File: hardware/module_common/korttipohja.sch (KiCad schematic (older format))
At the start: 6 parts

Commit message: Add root PCB for module design.
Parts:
- removed J?: Conn_01x07_Female, symbol Connector:Conn_01x07_Female
- removed J?: Conn_01x02_Female, symbol Connector:Conn_01x02_Female
- added U1: WAVGAT_CAN, WAVGAT_CAN:WAVGAT_CAN, symbol WAVGAT_CAN:WAVGAT_CAN
- J1: renamed from J?; footprint (none) -> Connector_RJ:RJ45_BEL_SS74301-00x_Vertical
- R1, R2: renamed from R?; footprint (none) -> Resistor_SMD:R_0603_1608Metric_Pad1.05x0.95mm_HandSolder
- gave numbers to parts that had none: 1
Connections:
- wire segments 51 -> 57
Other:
- moved on the sheet: A1, J1, R1, R2

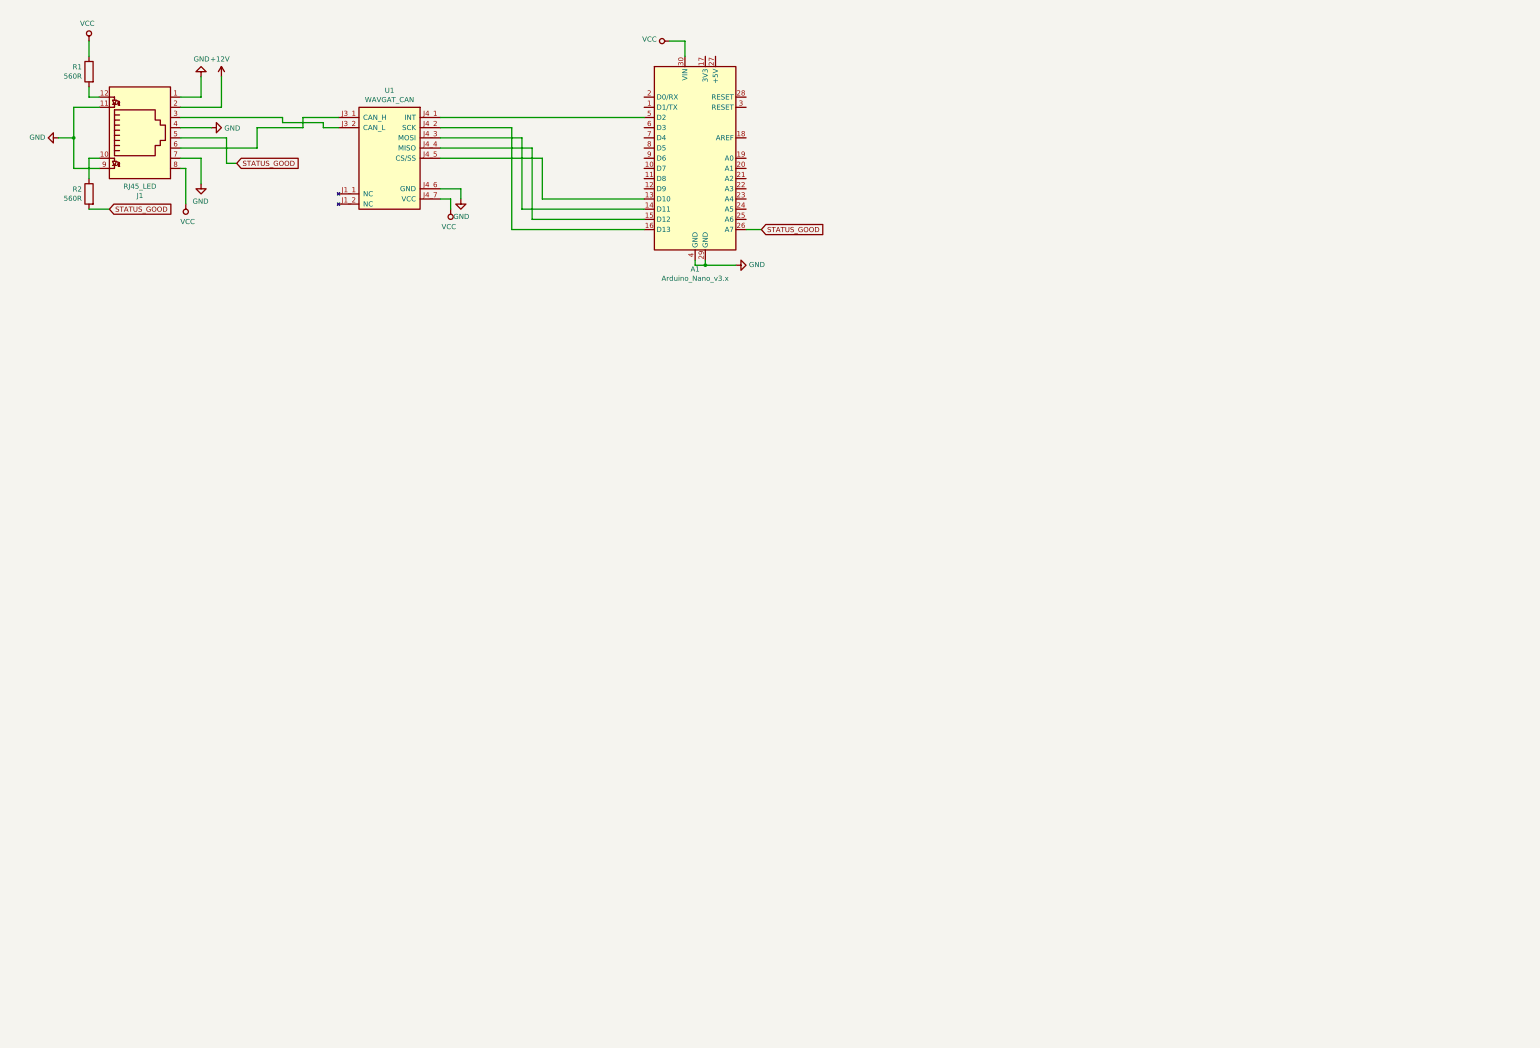
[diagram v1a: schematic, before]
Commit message: Finish first iteration of module common backplane
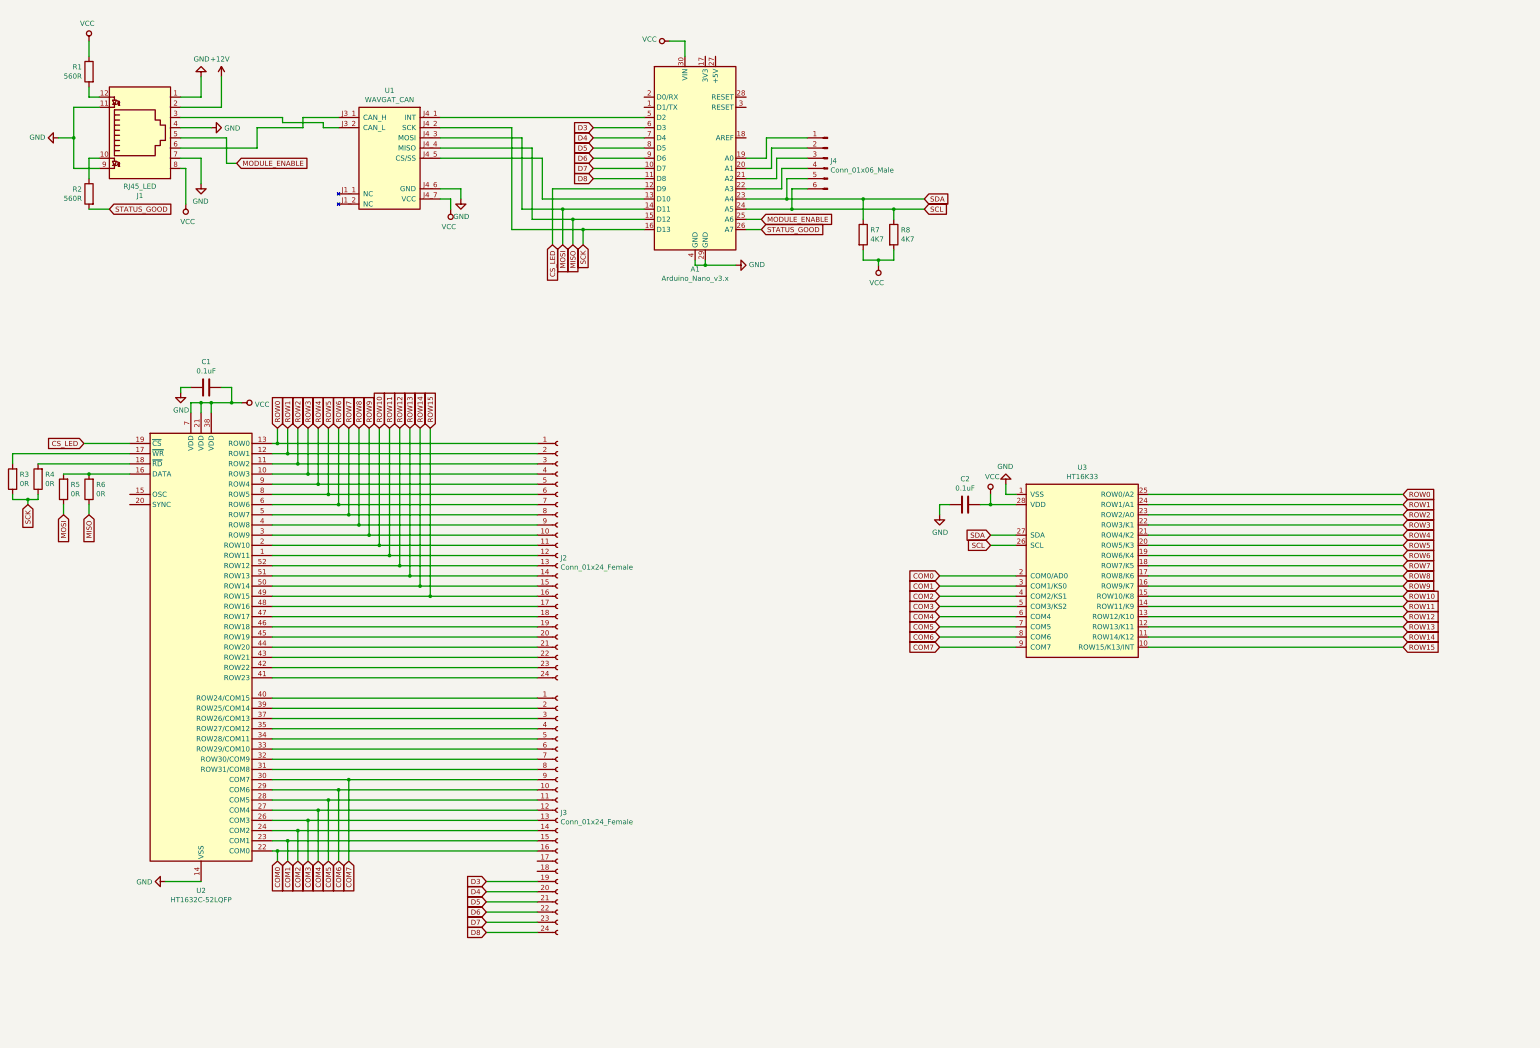
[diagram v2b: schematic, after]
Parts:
- added C1, C2: 0.1uF, Capacitor_SMD:C_0603_1608Metric_Pad1.05x0.95mm_HandSolder, symbol Device:C
- added J2, J3: Conn_01x24_Female, Connector_PinHeader_2.54mm:PinHeader_1x24_P2.54mm_Vertical, symbol Connector:Conn_01x24_Female
- added J4: Conn_01x06_Male, Connector_PinHeader_2.54mm:PinHeader_1x06_P2.54mm_Vertical, symbol Connector:Conn_01x06_Male
- added R3, R4, R5, R6: 0R, Resistor_SMD:R_0603_1608Metric_Pad1.05x0.95mm_HandSolder, symbol Device:R
- added R7, R8: 4K7, Resistor_SMD:R_0603_1608Metric_Pad1.05x0.95mm_HandSolder, symbol Device:R
- added U2: HT1632C-52LQFP, Package_QFP:LQFP-52_14x14mm_P1mm, symbol Driver_LED:HT1632C-52LQFP
- added U3: HT16K33, Package_SO:SOIC-28W_7.5x17.9mm_P1.27mm, symbol ProjectChips:HT16K33
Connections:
- net GND: now also C1.2, C2.2, U2.14 (VSS), U2.25 (VSS), U2.36 (VSS), U3.1 (VSS)
- net STATUS_GOOD: no longer J1.5
- net VCC: now also C1.1, C2.1, R7.2, R8.2, U2.21 (VDD), U2.38 (VDD), U2.7 (VDD), U3.28 (VDD)
- net D7: now reaches A1.10 (D7)
- net D7: now also J3.23 (Pin_23)
- net D8: now reaches A1.11 (D8)
- net D8: now also J3.24 (Pin_24)
- net CS_LED: now reaches A1.12 (D9)
- net CS_LED: now also U2.19 (~CS)
- net MOSI: now reaches A1.14 (D11), U1.J4_3 (MOSI)
- net MOSI: now also R5.1
- net MISO: now reaches A1.15 (D12), U1.J4_4 (MISO)
- net MISO: now also R6.1
- net SCK: now reaches A1.16 (D13), U1.J4_2 (SCK)
- net SCK: now also R3.1, R4.1
- net at A1.19 (A0): now also J4.1 (Pin_1)
- net at A1.20 (A1): now also J4.2 (Pin_2)
- net at A1.21 (A2): now also J4.3 (Pin_3)
- net at A1.22 (A3): now also J4.4 (Pin_4)
- net SDA: now reaches A1.23 (A4)
- net SDA: now also J4.5 (Pin_5), R7.1, U3.27 (SDA)
- net SCL: now reaches A1.24 (A5)
- net SCL: now also J4.6 (Pin_6), R8.1, U3.26 (SCL)
- net MODULE_ENABLE: now reaches A1.25 (A6)
- net MODULE_ENABLE: now also J1.5
- net D3: now reaches A1.6 (D3)
- net D3: now also J3.19 (Pin_19)
- net D4: now reaches A1.7 (D4)
- net D4: now also J3.20 (Pin_20)
- net D5: now reaches A1.8 (D5)
- net D5: now also J3.21 (Pin_21)
- net D6: now reaches A1.9 (D6)
- net D6: now also J3.22 (Pin_22)
- new net: R5.2, R6.2, U2.16 (DATA)
- new net: R3.2, U2.17 (~WR)
- new net: R4.2, U2.18 (~RD)
- new net: J3.8 (Pin_8), U2.31 (ROW31/COM8)
- new net: J3.7 (Pin_7), U2.32 (ROW30/COM9)
- new net: J3.6 (Pin_6), U2.33 (ROW29/COM10)
- new net: J3.5 (Pin_5), U2.34 (ROW28/COM11)
- new net: J3.4 (Pin_4), U2.35 (ROW27/COM12)
- new net: J3.3 (Pin_3), U2.37 (ROW26/COM13)
- new net: J3.2 (Pin_2), U2.39 (ROW25/COM14)
- new net: J3.1 (Pin_1), U2.40 (ROW24/COM15)
- new net: J2.24 (Pin_24), U2.41 (ROW23)
- new net: J2.23 (Pin_23), U2.42 (ROW22)
- new net: J2.22 (Pin_22), U2.43 (ROW21)
- new net: J2.21 (Pin_21), U2.44 (ROW20)
- new net: J2.20 (Pin_20), U2.45 (ROW19)
- new net: J2.19 (Pin_19), U2.46 (ROW18)
- new net: J2.18 (Pin_18), U2.47 (ROW17)
- new net: J2.17 (Pin_17), U2.48 (ROW16)
- new net COM0: J3.16 (Pin_16), U2.22 (COM0), U3.2 (COM0/AD0)
- new net COM1: J3.15 (Pin_15), U2.23 (COM1), U3.3 (COM1/KS0)
- new net COM2: J3.14 (Pin_14), U2.24 (COM2), U3.4 (COM2/KS1)
- new net COM3: J3.13 (Pin_13), U2.26 (COM3), U3.5 (COM3/KS2)
- new net COM4: J3.12 (Pin_12), U2.27 (COM4), U3.6 (COM4)
- new net COM5: J3.11 (Pin_11), U2.28 (COM5), U3.7 (COM5)
- new net COM6: J3.10 (Pin_10), U2.29 (COM6), U3.8 (COM6)
- new net COM7: J3.9 (Pin_9), U2.30 (COM7), U3.9 (COM7)
- new net ROW0: J2.1 (Pin_1), U2.13 (ROW0), U3.25 (ROW0/A2)
- new net ROW1: J2.2 (Pin_2), U2.12 (ROW1), U3.24 (ROW1/A1)
- new net ROW10: J2.11 (Pin_11), U2.2 (ROW10), U3.15 (ROW10/K8)
- new net ROW11: J2.12 (Pin_12), U2.1 (ROW11), U3.14 (ROW11/K9)
- new net ROW12: J2.13 (Pin_13), U2.52 (ROW12), U3.13 (ROW12/K10)
- new net ROW13: J2.14 (Pin_14), U2.51 (ROW13), U3.12 (ROW13/K11)
- new net ROW14: J2.15 (Pin_15), U2.50 (ROW14), U3.11 (ROW14/K12)
- new net ROW15: J2.16 (Pin_16), U2.49 (ROW15), U3.10 (ROW15/K13/INT)
- new net ROW2: J2.3 (Pin_3), U2.11 (ROW2), U3.23 (ROW2/A0)
- new net ROW3: J2.4 (Pin_4), U2.10 (ROW3), U3.22 (ROW3/K1)
- new net ROW4: J2.5 (Pin_5), U2.9 (ROW4), U3.21 (ROW4/K2)
- new net ROW5: J2.6 (Pin_6), U2.8 (ROW5), U3.20 (ROW5/K3)
- new net ROW6: J2.7 (Pin_7), U2.6 (ROW6), U3.19 (ROW6/K4)
- new net ROW7: J2.8 (Pin_8), U2.5 (ROW7), U3.18 (ROW7/K5)
- new net ROW8: J2.9 (Pin_9), U2.4 (ROW8), U3.17 (ROW8/K6)
- new net ROW9: J2.10 (Pin_10), U2.3 (ROW9), U3.16 (ROW9/K7)

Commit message: Add +5V and +12V to module funcitonal PCB.
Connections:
- net +12V: now also J3.18 (Pin_18)
- net VCC: now also J3.17 (Pin_17)
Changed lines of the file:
@@
 Wire Wire Line
 	5200 9800 5700 9800
+$Comp
+L power:VCC #PWR?
+U 1 1 5DD3D5CD
+P 5650 9100
+F 0 "#PWR?" H 5650 8950 50  0001 C CNN
+F 1 "VCC" V 5668 9227 50  0000 L CNN
+F 2 "" H 5650 9100 50  0001 C CNN
+F 3 "" H 5650 9100 50  0001 C CNN
+	1    5650 9100
+	0    -1   -1   0
+$EndComp
+$Comp
+L power:+12V #PWR?
+U 1 1 5DD3E2FF
+P 5650 9200
+F 0 "#PWR?" H 5650 9050 50  0001 C CNN
+F 1 "+12V" V 5665 9328 50  0000 L CNN
+F 2 "" H 5650 9200 50  0001 C CNN
+F 3 "" H 5650 9200 50  0001 C CNN
+	1    5650 9200
+	0    -1   -1   0
+$EndComp
+Wire Wire Line
+	5650 9100 5700 9100
+Wire Wire Line
+	5700 9200 5650 9200
 $EndSCHEMATC

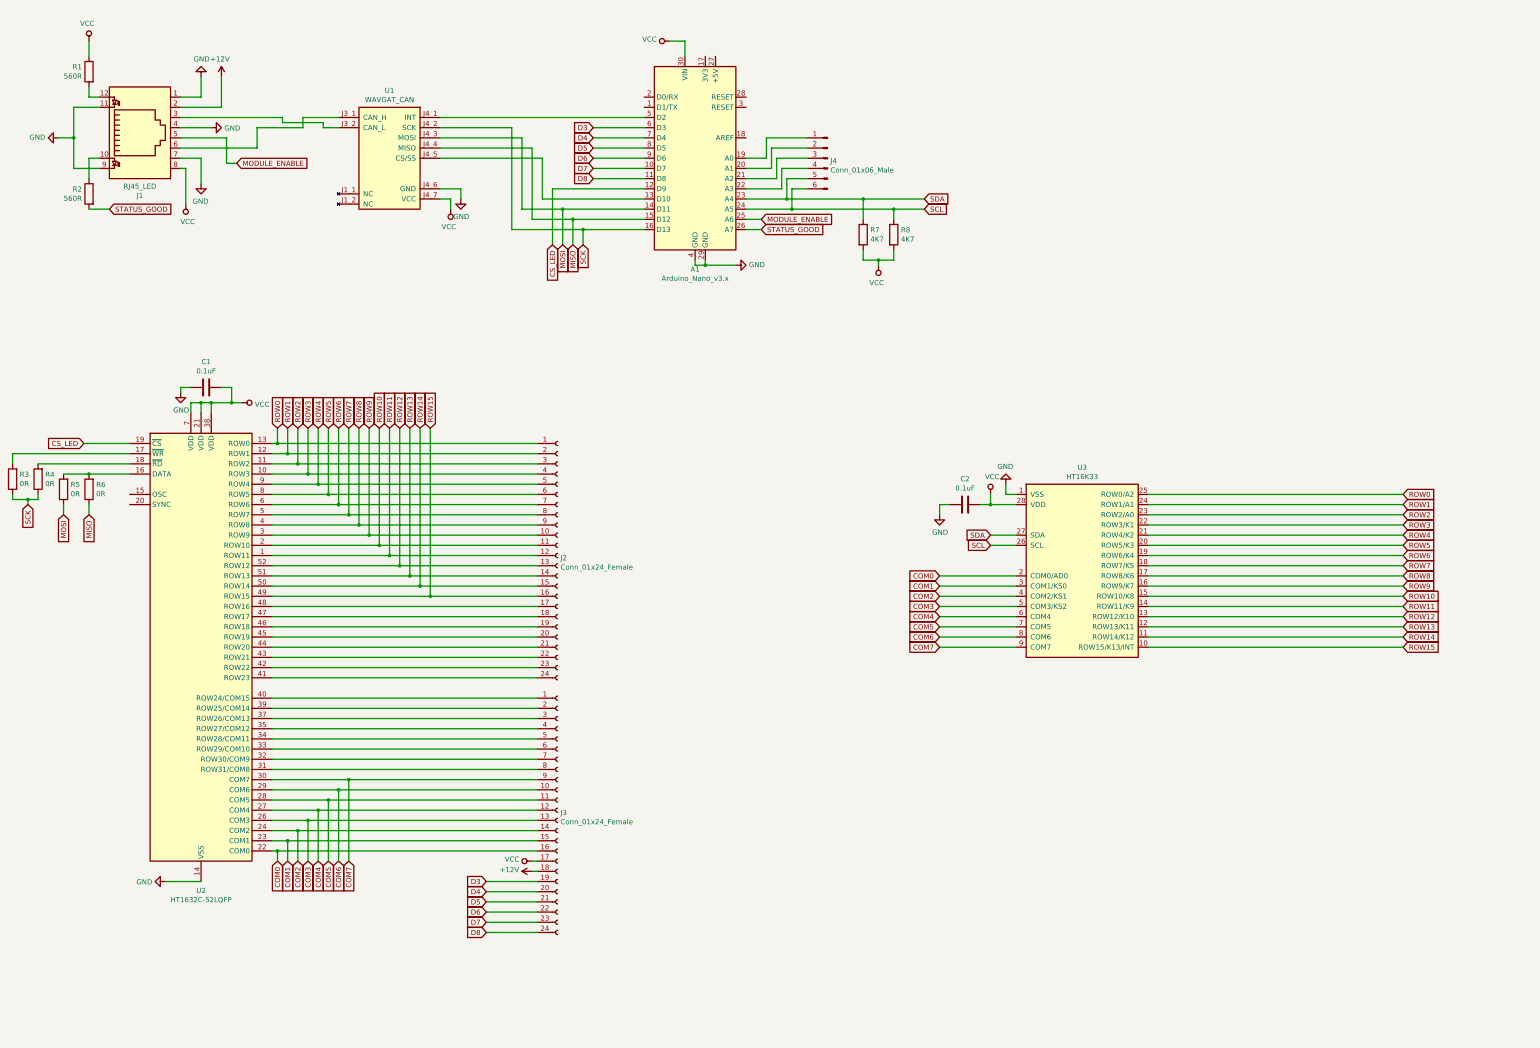
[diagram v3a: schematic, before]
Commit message: Add FETs for increased current control.
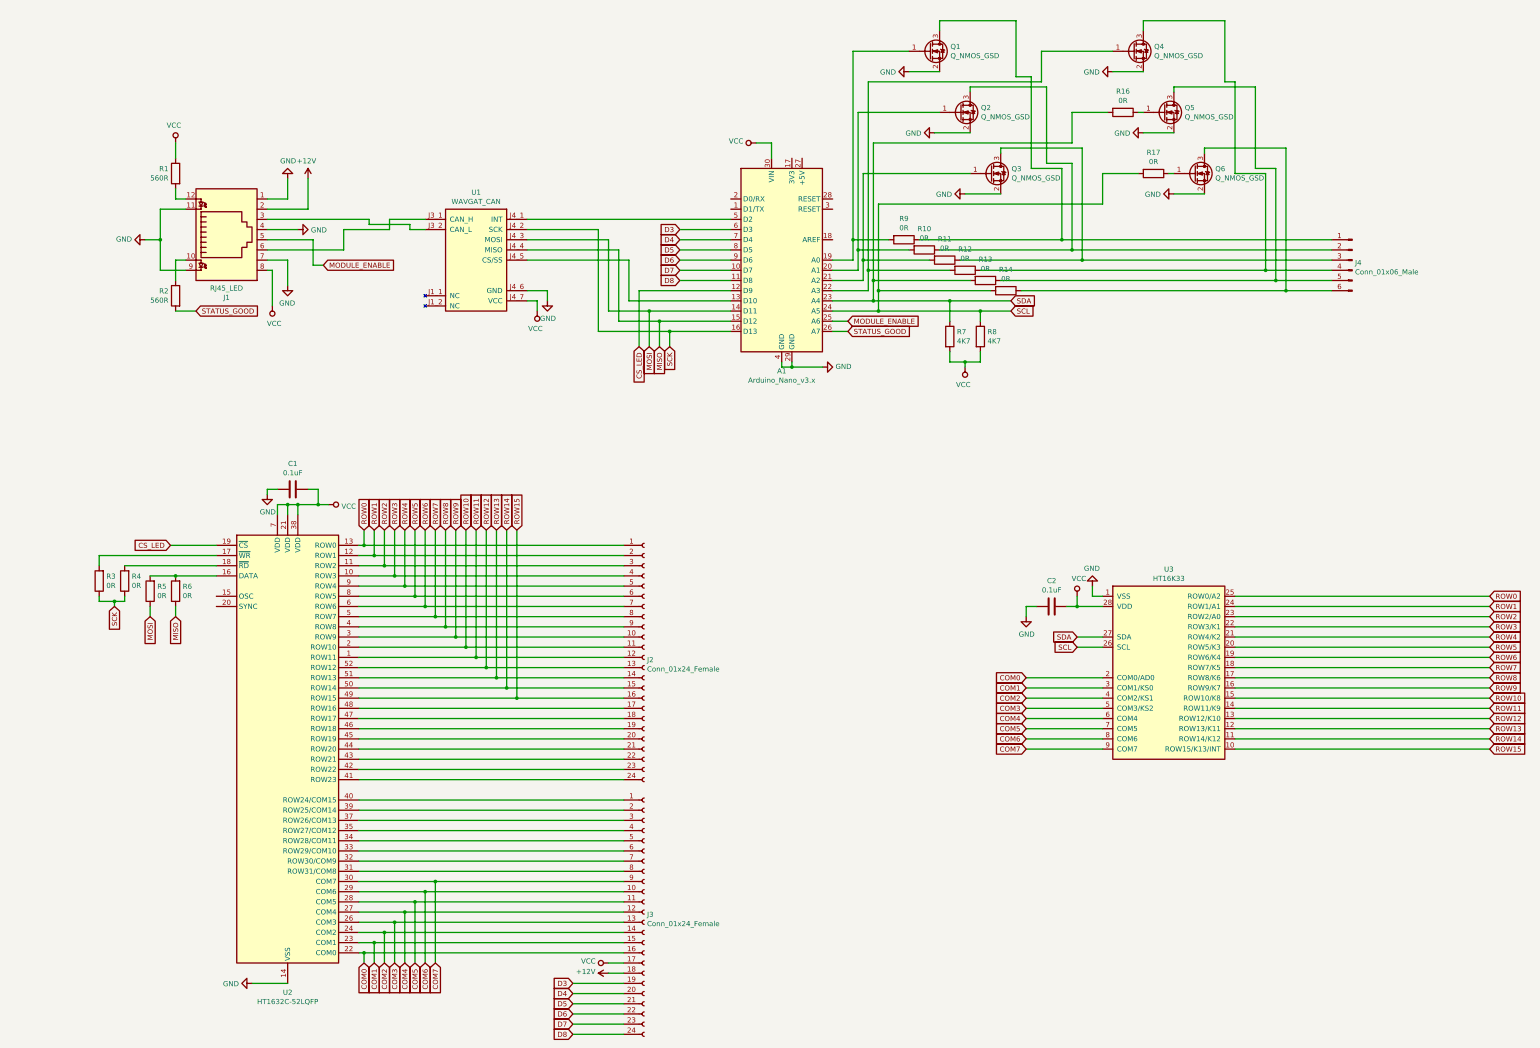
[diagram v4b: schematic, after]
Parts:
- added Q1, Q2, Q3, Q4, Q5, Q6: Q_NMOS_GSD, Package_TO_SOT_SMD:SOT-23, symbol Device:Q_NMOS_GSD
- added R10, R11, R12, R13, R14, R16, R17, R9: 0R, Resistor_SMD:R_0603_1608Metric_Pad1.05x0.95mm_HandSolder, symbol Device:R
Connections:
- net GND: now also Q1.2 (S), Q2.2 (S), Q3.2 (S), Q4.2 (S), Q5.2 (S), Q6.2 (S)
- net SCL: now also R14.2, R17.2; no longer J4.6 (Pin_6)
- net SDA: now also R13.2, R16.2; no longer J4.5 (Pin_5)
- net at A1.19 (A0): now also Q1.1 (G), R9.2; no longer J4.1 (Pin_1)
- net at A1.20 (A1): now also Q2.1 (G), R10.2; no longer J4.2 (Pin_2)
- net at A1.21 (A2): now also Q3.1 (G), R11.2; no longer J4.3 (Pin_3)
- net at A1.22 (A3): now also Q4.1 (G), R12.2; no longer J4.4 (Pin_4)
- new net: J4.1 (Pin_1), Q1.3 (D), R9.1
- new net: J4.2 (Pin_2), Q2.3 (D), R10.1
- new net: J4.3 (Pin_3), Q3.3 (D), R11.1
- new net: J4.4 (Pin_4), Q4.3 (D), R12.1
- new net: Q5.1 (G), R16.1
- new net: J4.5 (Pin_5), Q5.3 (D), R13.1
- new net: Q6.1 (G), R17.1
- new net: J4.6 (Pin_6), Q6.3 (D), R14.1
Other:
- moved on the sheet: A1, C1, C2, J1, J2, J3, J4, R1, R2, R3, R4, R5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

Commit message: Add timer adapter pcb
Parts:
- A1: symbol MCU_Module:Arduino_Nano_v3.x -> korttipohja-rescue:Arduino_Nano_v3.x-MCU_Module
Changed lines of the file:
@@
 EESchema Schematic File Version 4
-LIBS:korttipohja-cache
 EELAYER 30 0
 EELAYER END
@@
 $EndDescr
 $Comp
-L MCU_Module:Arduino_Nano_v3.x A1
+L korttipohja-rescue:Arduino_Nano_v3.x-MCU_Module A1
 U 1 1 5D938166
 P 8100 3200
